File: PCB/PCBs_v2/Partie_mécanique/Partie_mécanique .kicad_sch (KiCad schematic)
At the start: 21 parts, among them J1 Conn_01x04, J10 Conn_01x02, J2 Conn_01x04, J3 BU33SD5WG-TR, J4 R-78B5.0-2.0, J5 Conn_01x04, J7 Conn_01x04, J9 Conn_01x02

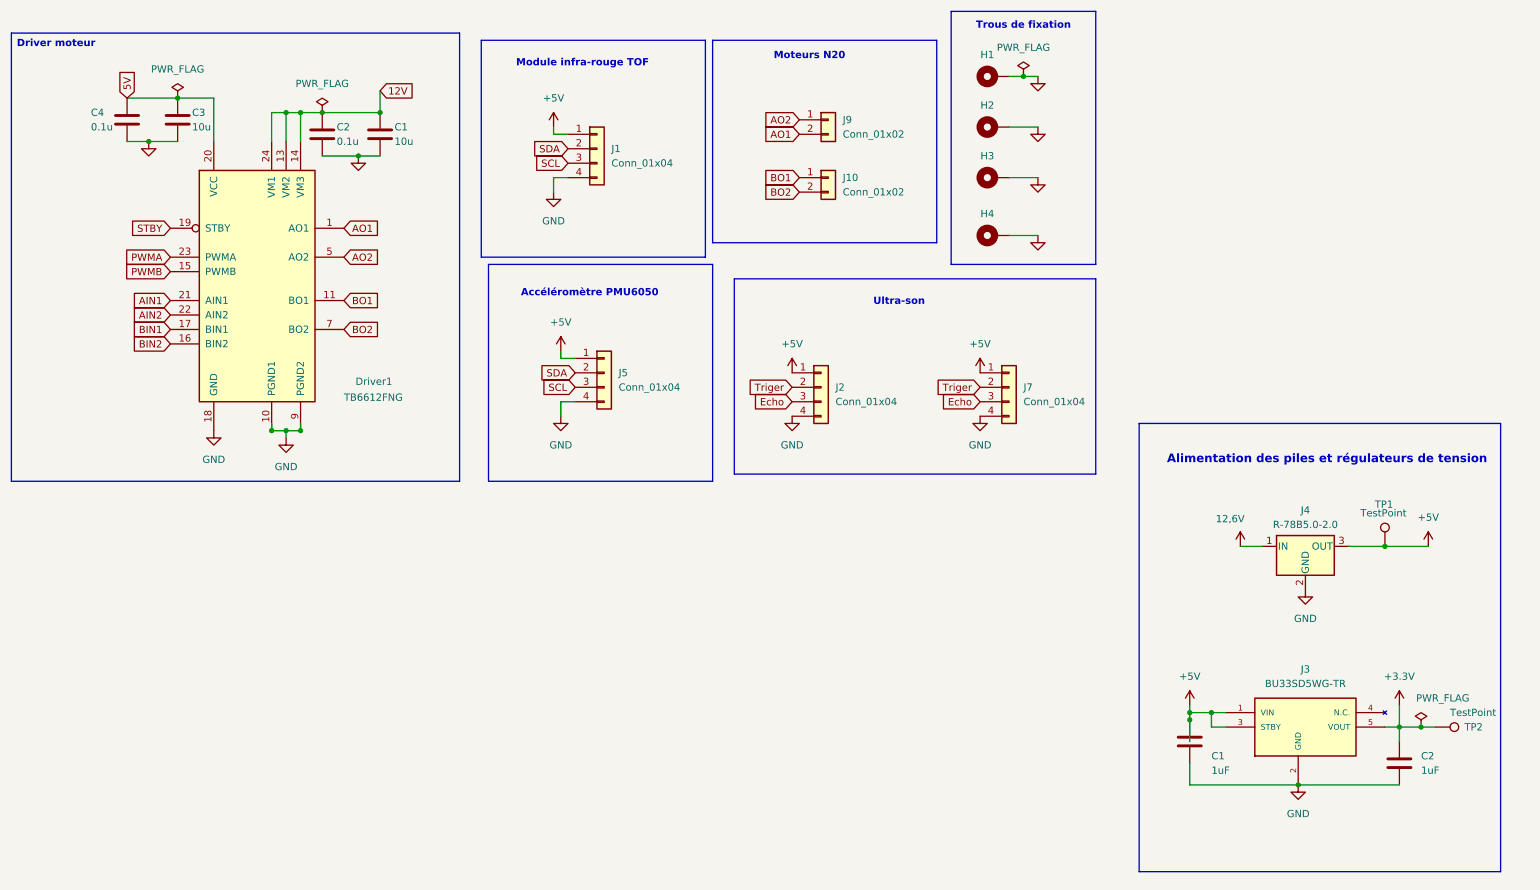
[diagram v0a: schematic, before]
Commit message: fin schéma + Routage PCB cmd
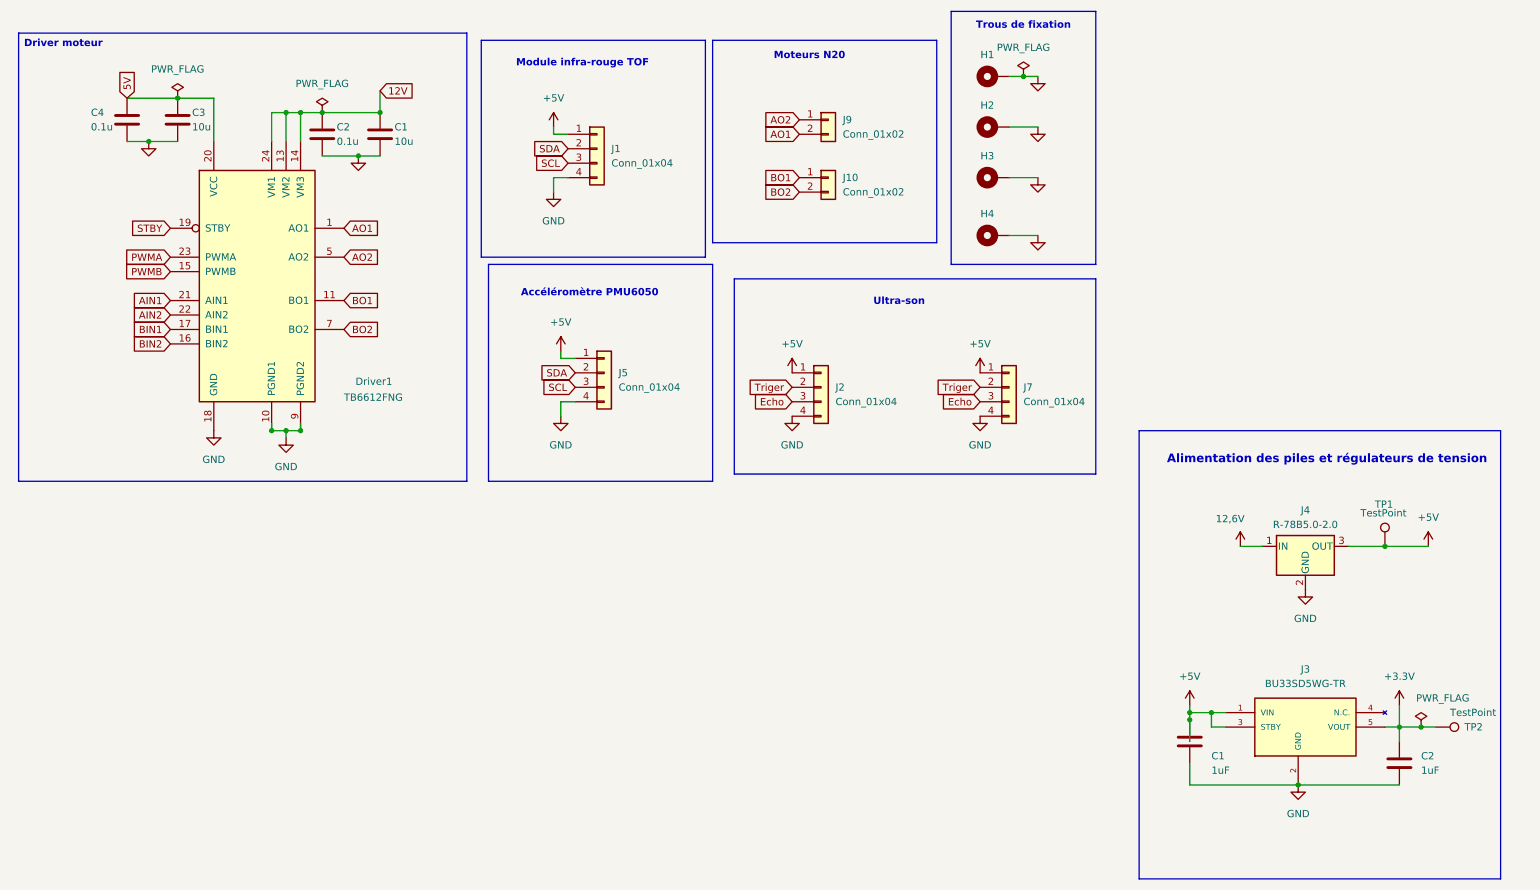
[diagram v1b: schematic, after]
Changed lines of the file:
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@@
 	)
 	(rectangle
-		(start 218.44 86.36)
-		(end 281.94 165.1)
+		(start 218.44 87.63)
+		(end 281.94 166.37)
 		(stroke
 			(width 0)
@@
 	(text_box "Driver moteur"
 		(exclude_from_sim no)
-		(at 20.32 17.78 0)
+		(at 21.59 17.78 0)
 		(size 78.74 78.74)
 		(margins 0.9525 0.9525 0.9525 0.9525)
